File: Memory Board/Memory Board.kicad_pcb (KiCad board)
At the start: 4 copper layers, 29.8 x 38.1 mm, 39 parts, among them IC2 MCP2557FDT-H_MNY, J1 USB4056-03-A_REVA2, J2 Conn_01x04_Socket, J3 Conn_01x04_Socket, J4 Conn_01x04_Socket, SW1 SW_SPST, SW2 SW_SPDT, U1 STM32G473CBTx, U2 LD1117S33TR_SOT223, X1 ECS-2520MV-xxx-xx

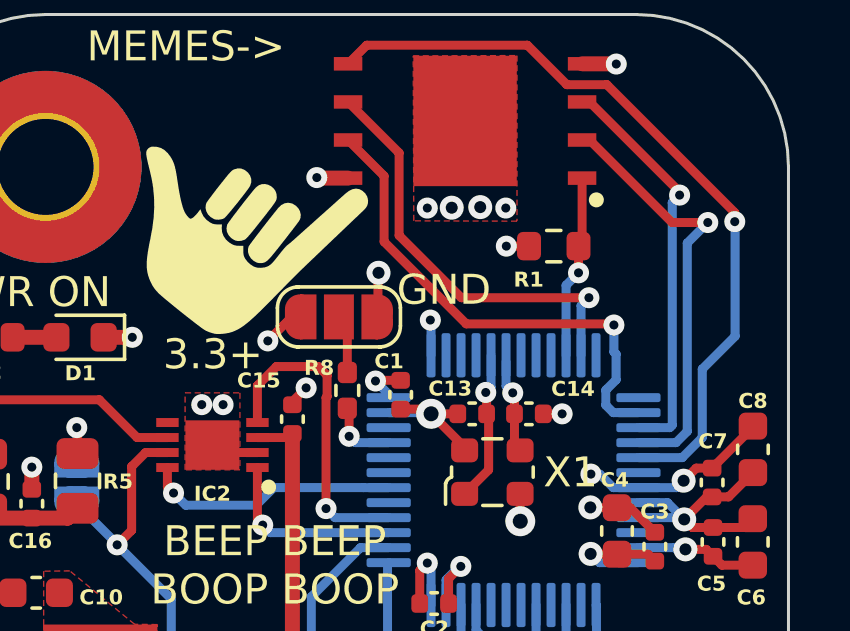
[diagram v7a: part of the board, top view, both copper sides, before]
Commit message: Revised good mems
https://www.digikey.com/short/14vp1r7m
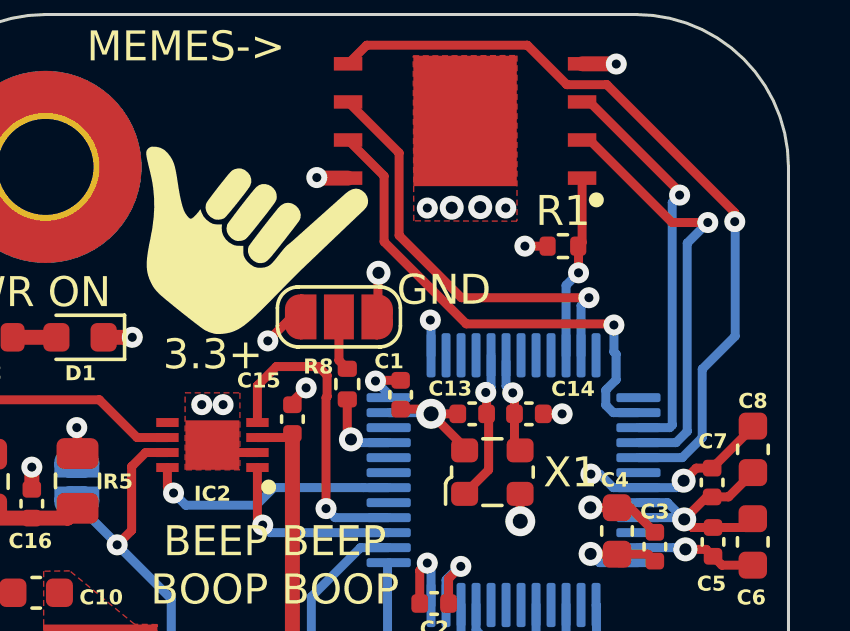
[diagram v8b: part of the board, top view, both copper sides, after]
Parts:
- R1: footprint Resistor_SMD:R_0603_1608Metric -> Resistor_SMD:R_0402_1005Metric
- R8: footprint Resistor_SMD:R_0402_1005Metric_Pad0.72x0.64mm_HandSolder -> Resistor_SMD:R_0402_1005Metric
- moved R1 0.30 mm to (47.7, 33.1)
- moved R8 0.21 mm to (40.5, 37.7)
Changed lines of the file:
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@@
     )
   )
-  (footprint "Resistor_SMD:R_0402_1005Metric_Pad0.72x0.64mm_HandSolder" (layer "F.Cu")
-    (at 40.54 37.93 -90)
-    (descr "Resistor SMD 0402 (1005 Metric), square (rectangular) end terminal, IPC_7351 nominal with elongated pad for handsoldering. (Body size source: IPC-SM-782 page 72, https://www.pcb-3d.com/wordpress/wp-content/uploads/ipc-sm-782a_amendment_1_and_2.pdf), generated with kicad-footprint-generator")
-    (tags "resistor handsolder")
+  (footprint "Resistor_SMD:R_0402_1005Metric" (layer "F.Cu")
+    (at 40.5384 37.719 -90)
+    (descr "Resistor SMD 0402 (1005 Metric), square (rectangular) end terminal, IPC_7351 nominal, (Body size source: IPC-SM-782 page 72, https://www.pcb-3d.com/wordpress/wp-content/uploads/ipc-sm-782a_amendment_1_and_2.pdf), generated with kicad-footprint-generator")
+    (tags "resistor")
     (property "Sheetfile" "Memory Board.kicad_sch")
     (property "Sheetname" "")
@@
     (property "ki_keywords" "R res resistor")
     (attr smd)
-    (fp_text reference "R8" (at -0.75 0.94) (layer "F.SilkS")
+    (fp_text reference "R8" (at -0.5842 0.9652 180) (layer "F.SilkS")
         (effects (font (size 0.5 0.5) (thickness 0.1) bold))
     )
-    (fp_text value "10k" (at 0 1.17 90) (layer "F.Fab")
+    (fp_text value "10k" (at 0 1.17 -90) (layer "F.Fab")
         (effects (font (size 1 1) (thickness 0.15)))
     )
-    (fp_text user "${REFERENCE}" (at 0 0 90) (layer "F.Fab")
+    (fp_text user "${REFERENCE}" (at 0 0 -90) (layer "F.Fab")
         (effects (font (size 0.26 0.26) (thickness 0.04)))
     )
-    (fp_line (start -0.167621 -0.38) (end 0.167621 -0.38)
+    (fp_line (start -0.153641 -0.38) (end 0.153641 -0.38)
       (stroke (width 0.12) (type solid)) (layer "F.SilkS"))
-    (fp_line (start -0.167621 0.38) (end 0.167621 0.38)
+    (fp_line (start -0.153641 0.38) (end 0.153641 0.38)
       (stroke (width 0.12) (type solid)) (layer "F.SilkS"))
-    (fp_line (start -1.1 -0.47) (end 1.1 -0.47)
+    (fp_line (start -0.93 -0.47) (end 0.93 -0.47)
       (stroke (width 0.05) (type solid)) (layer "F.CrtYd"))
-    (fp_line (start -1.1 0.47) (end -1.1 -0.47)
+    (fp_line (start -0.93 0.47) (end -0.93 -0.47)
       (stroke (width 0.05) (type solid)) (layer "F.CrtYd"))
-    (fp_line (start 1.1 -0.47) (end 1.1 0.47)
+    (fp_line (start 0.93 -0.47) (end 0.93 0.47)
       (stroke (width 0.05) (type solid)) (layer "F.CrtYd"))
-    (fp_line (start 1.1 0.47) (end -1.1 0.47)
+    (fp_line (start 0.93 0.47) (end -0.93 0.47)
       (stroke (width 0.05) (type solid)) (layer "F.CrtYd"))
     (fp_line (start -0.525 -0.27) (end 0.525 -0.27)
@@
     (fp_line (start 0.525 0.27) (end -0.525 0.27)
       (stroke (width 0.1) (type solid)) (layer "F.Fab"))
-    (pad "1" smd roundrect (at -0.5975 0 270) (size 0.715 0.64) (layers "F.Cu" "F.Paste" "F.Mask") (roundrect_rratio 0.25)
+    (pad "1" smd roundrect (at -0.51 0 270) (size 0.54 0.64) (layers "F.Cu" "F.Paste" "F.Mask") (roundrect_rratio 0.25)
       (net 65 "Net-(SW2-B)") (pintype "passive"))
-    (pad "2" smd roundrect (at 0.5975 0 270) (size 0.715 0.64) (layers "F.Cu" "F.Paste" "F.Mask") (roundrect_rratio 0.25)
+    (pad "2" smd roundrect (at 0.51 0 270) (size 0.54 0.64) (layers "F.Cu" "F.Paste" "F.Mask") (roundrect_rratio 0.25)
       (net 64 "/BOOT0") (pintype "passive"))
     (model "${KICAD6_3DMODEL_DIR}/Resistor_SMD.3dshapes/R_0402_1005Metric.wrl"
@@
     )
   )
-  (footprint "Resistor_SMD:R_0603_1608Metric" (layer "F.Cu")
-    (at 47.4218 33.1216)
-    (descr "Resistor SMD 0603 (1608 Metric), square (rectangular) end terminal, IPC_7351 nominal, (Body size source: IPC-SM-782 page 72, https://www.pcb-3d.com/wordpress/wp-content/uploads/ipc-sm-782a_amendment_1_and_2.pdf), generated with kicad-footprint-generator")
+  (footprint "Resistor_SMD:R_0402_1005Metric" (layer "F.Cu")
+    (at 47.7266 33.1216)
+    (descr "Resistor SMD 0402 (1005 Metric), square (rectangular) end terminal, IPC_7351 nominal, (Body size source: IPC-SM-782 page 72, https://www.pcb-3d.com/wordpress/wp-content/uploads/ipc-sm-782a_amendment_1_and_2.pdf), generated with kicad-footprint-generator")
     (tags "resistor")
     (property "Sheetfile" "Memory Board.kicad_sch")
@@
     (property "ki_keywords" "R resistor")
     (attr smd)
-    (fp_text reference "R1" (at -0.8382 1.1176) (layer "F.SilkS")
-        (effects (font (size 0.5 0.5) (thickness 0.1) bold))
+    (fp_text reference "R1" (at 0 -1.17) (layer "F.SilkS")
+        (effects (font (size 1 1) (thickness 0.15)))
     )
-    (fp_text value "10k" (at 0 1.43) (layer "F.Fab")
+    (fp_text value "10k" (at 0 1.17) (layer "F.Fab")
         (effects (font (size 1 1) (thickness 0.15)))
     )
     (fp_text user "${REFERENCE}" (at 0 0) (layer "F.Fab")
-        (effects (font (size 0.4 0.4) (thickness 0.06)))
+        (effects (font (size 0.26 0.26) (thickness 0.04)))
     )
-    (fp_line (start -0.237258 -0.5225) (end 0.237258 -0.5225)
+    (fp_line (start -0.153641 -0.38) (end 0.153641 -0.38)
       (stroke (width 0.12) (type solid)) (layer "F.SilkS"))
-    (fp_line (start -0.237258 0.5225) (end 0.237258 0.5225)
+    (fp_line (start -0.153641 0.38) (end 0.153641 0.38)
       (stroke (width 0.12) (type solid)) (layer "F.SilkS"))
-    (fp_line (start -1.48 -0.73) (end 1.48 -0.73)
+    (fp_line (start -0.93 -0.47) (end 0.93 -0.47)
       (stroke (width 0.05) (type solid)) (layer "F.CrtYd"))
-    (fp_line (start -1.48 0.73) (end -1.48 -0.73)
+    (fp_line (start -0.93 0.47) (end -0.93 -0.47)
       (stroke (width 0.05) (type solid)) (layer "F.CrtYd"))
-    (fp_line (start 1.48 -0.73) (end 1.48 0.73)
+    (fp_line (start 0.93 -0.47) (end 0.93 0.47)
       (stroke (width 0.05) (type solid)) (layer "F.CrtYd"))
-    (fp_line (start 1.48 0.73) (end -1.48 0.73)
+    (fp_line (start 0.93 0.47) (end -0.93 0.47)
       (stroke (width 0.05) (type solid)) (layer "F.CrtYd"))
-    (fp_line (start -0.8 -0.4125) (end 0.8 -0.4125)
+    (fp_line (start -0.525 -0.27) (end 0.525 -0.27)
       (stroke (width 0.1) (type solid)) (layer "F.Fab"))
-    (fp_line (start -0.8 0.4125) (end -0.8 -0.4125)
+    (fp_line (start -0.525 0.27) (end -0.525 -0.27)
       (stroke (width 0.1) (type solid)) (layer "F.Fab"))
-    (fp_line (start 0.8 -0.4125) (end 0.8 0.4125)
+    (fp_line (start 0.525 -0.27) (end 0.525 0.27)
       (stroke (width 0.1) (type solid)) (layer "F.Fab"))
-    (fp_line (start 0.8 0.4125) (end -0.8 0.4125)
+    (fp_line (start 0.525 0.27) (end -0.525 0.27)
       (stroke (width 0.1) (type solid)) (layer "F.Fab"))
-    (pad "1" smd roundrect (at -0.825 0) (size 0.8 0.95) (layers "F.Cu" "F.Paste" "F.Mask") (roundrect_rratio 0.25)
+    (pad "1" smd roundrect (at -0.51 0) (size 0.54 0.64) (layers "F.Cu" "F.Paste" "F.Mask") (roundrect_rratio 0.25)
       (net 1 "+3.3V") (pintype "passive"))
-    (pad "2" smd roundrect (at 0.825 0) (size 0.8 0.95) (layers "F.Cu" "F.Paste" "F.Mask") (roundrect_rratio 0.25)
+    (pad "2" smd roundrect (at 0.51 0) (size 0.54 0.64) (layers "F.Cu" "F.Paste" "F.Mask") (roundrect_rratio 0.25)
       (net 8 "QUADSPI_NCS") (pintype "passive"))
-    (model "${KICAD6_3DMODEL_DIR}/Resistor_SMD.3dshapes/R_0603_1608Metric.wrl"
+    (model "${KICAD6_3DMODEL_DIR}/Resistor_SMD.3dshapes/R_0402_1005Metric.wrl"
       (offset (xyz 0 0 0))
       (scale (xyz 1 1 1))
@@
   (segment (start 42.954 45.0342) (end 42.954 43.936352) (width 0.3) (layer "F.Cu") (net 1))
   (segment (start 53.25 41.48) (end 52.7 41.48) (width 0.3) (layer "F.Cu") (net 1))
-  (segment (start 46.5968 33.1216) (end 45.84 33.1216) (width 0.3) (layer "F.Cu") (net 1))
+  (segment (start 47.216 33.1216) (end 46.4592 33.1216) (width 0.3) (layer "F.Cu") (net 1))
   (segment (start 38.96 35.48) (end 38.69 35.48) (width 0.25) (layer "F.Cu") (net 1))
   (segment (start 43.47 47.7) (end 43.4594 47.7106) (width 0.5) (layer "F.Cu") (net 1))
@@
   (via (at 31.0134 48.5394) (size 1) (drill 0.5) (layers "F.Cu" "B.Cu") (free) (net 1))
   (via (at 43.307 35.5854) (size 0.7) (drill 0.3) (layers "F.Cu" "B.Cu") (net 1))
-  (via (at 45.84 33.1216) (size 0.7) (drill 0.3) (layers "F.Cu" "B.Cu") (net 1))
+  (via (at 46.4592 33.1216) (size 0.7) (drill 0.3) (layers "F.Cu" "B.Cu") (net 1))
   (via (at 43.47 47.7) (size 0.7) (drill 0.3) (layers "F.Cu" "B.Cu") (net 1))
   (via (at 43.2053 43.685052) (size 0.7) (drill 0.3) (layers "F.Cu" "B.Cu") (net 1))
@@
   (segment (start 37.720217 42.420374) (end 37.970843 42.671) (width 0.3) (layer "B.Cu") (net 59))
   (segment (start 37.970843 42.671) (end 41.9183 42.671) (width 0.3) (layer "B.Cu") (net 59))
-  (segment (start 40.6 39.46) (end 40.6 38.5875) (width 0.3) (layer "F.Cu") (net 64))
-  (segment (start 40.6 38.5875) (end 40.54 38.5275) (width 0.3) (layer "F.Cu") (net 64))
-  (via (at 40.6 39.46) (size 0.7) (drill 0.3) (layers "F.Cu" "B.Cu") (net 64))
-  (segment (start 41.9183 39.671) (end 40.811 39.671) (width 0.3) (layer "B.Cu") (net 64))
-  (segment (start 40.811 39.671) (end 40.6 39.46) (width 0.3) (layer "B.Cu") (net 64))
+  (segment (start 40.5384 39.441339) (end 40.660856 39.563795) (width 0.3) (layer "F.Cu") (net 64))
+  (segment (start 40.5384 38.229) (end 40.5384 39.441339) (width 0.3) (layer "F.Cu") (net 64))
+  (via (at 40.660856 39.563795) (size 0.8) (drill 0.4) (layers "F.Cu" "B.Cu") (net 64))
+  (segment (start 40.660856 39.563795) (end 40.768061 39.671) (width 0.3) (layer "B.Cu") (net 64))
+  (segment (start 40.768061 39.671) (end 41.9183 39.671) (width 0.3) (layer "B.Cu") (net 64))
   (segment (start 40.54 35.76) (end 40.26 35.48) (width 0.3) (layer "F.Cu") (net 65))
-  (segment (start 40.54 37.3325) (end 40.54 35.76) (width 0.3) (layer "F.Cu") (net 65))
+  (segment (start 40.26 36.9306) (end 40.5384 37.209) (width 0.3) (layer "F.Cu") (net 65))
+  (segment (start 40.26 35.48) (end 40.26 36.9306) (width 0.3) (layer "F.Cu") (net 65))
   (zone (net 1) (net_name "+3.3V") (layer "F.Cu") (hatch edge 0.5)
     (priority 3)
